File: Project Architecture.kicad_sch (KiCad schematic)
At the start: 32 parts, among them J1 Screw_Terminal_01x04, U1 TMP102xxDRL

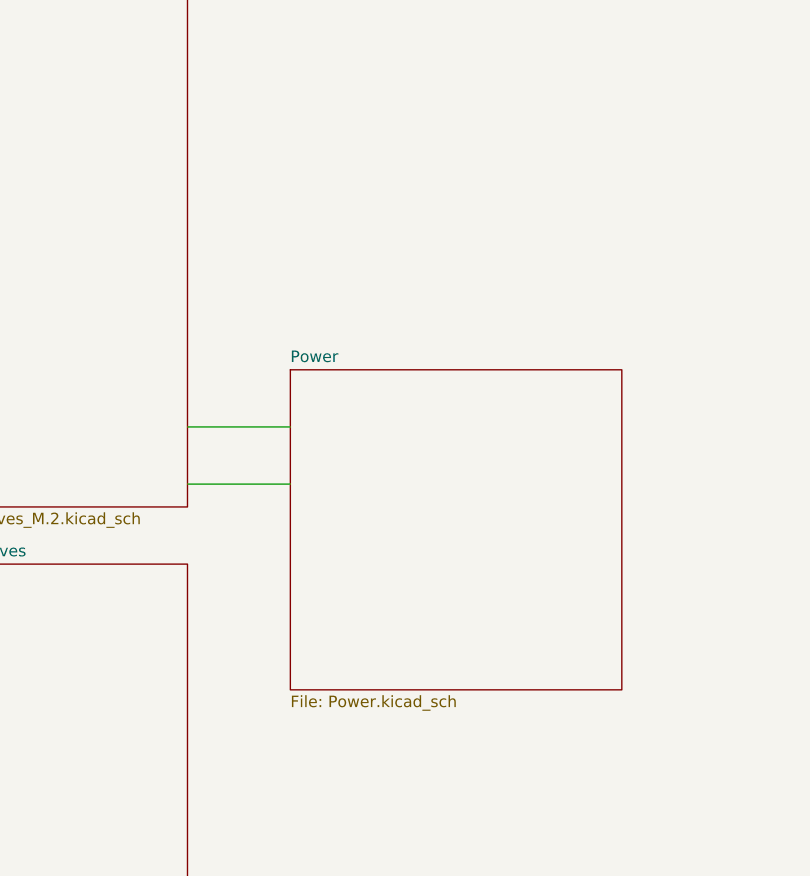
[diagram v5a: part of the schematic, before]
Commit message: Notation changed on M.2 Sheet
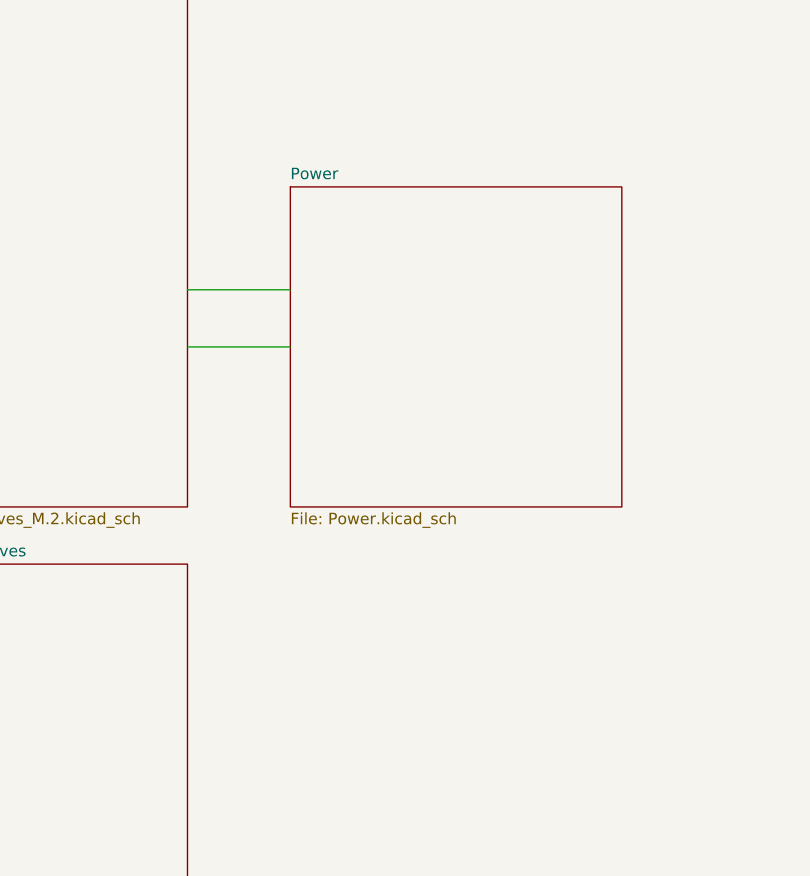
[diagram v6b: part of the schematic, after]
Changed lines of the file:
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@@
 	(wire
 		(pts
-			(xy 287.02 88.9) (xy 298.45 88.9)
+			(xy 287.02 73.66) (xy 298.45 73.66)
 		)
 		(stroke
@@
 	(wire
 		(pts
-			(xy 287.02 82.55) (xy 298.45 82.55)
+			(xy 287.02 67.31) (xy 298.45 67.31)
 		)
 		(stroke
@@
 	)
 	(sheet
-		(at 298.45 76.2)
+		(at 298.45 55.88)
 		(size 36.83 35.56)
 		(exclude_from_sim no)
@@
 		)
 		(property "Sheetname" "Power"
-			(at 298.45 75.4884 0)
+			(at 298.45 55.1684 0)
 			(effects
 				(font
@@
 		)
 		(property "Sheetfile" "Power.kicad_sch"
-			(at 298.45 112.3446 0)
+			(at 298.45 92.0246 0)
 			(effects
 				(font

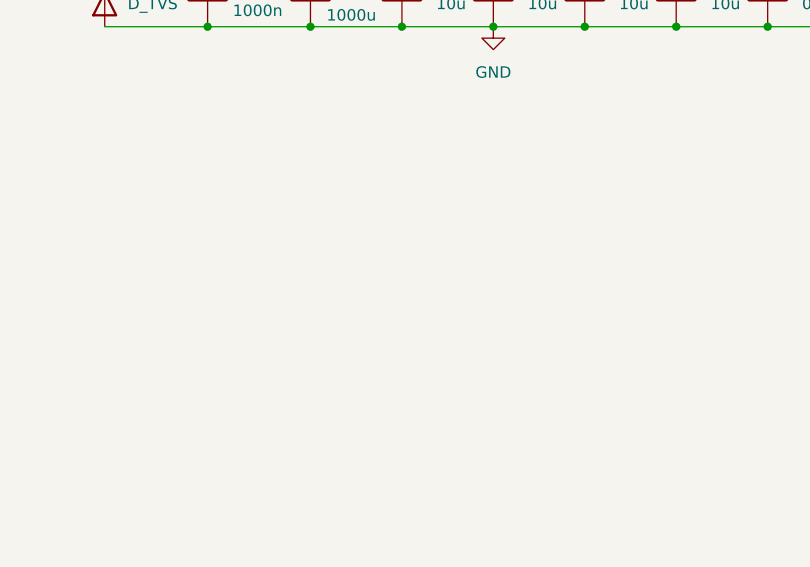
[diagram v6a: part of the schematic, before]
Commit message: Started Ethernet design
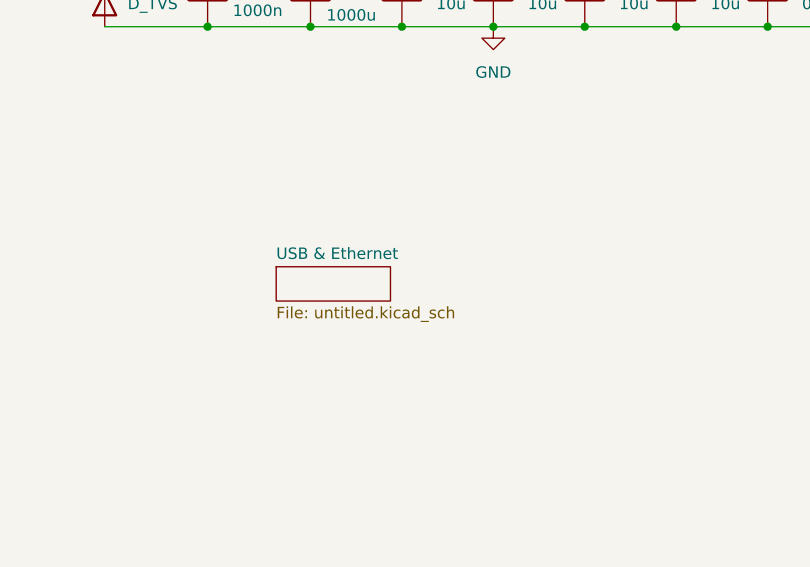
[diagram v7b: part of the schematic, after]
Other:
- added sheet USB & Ethernet (untitled.kicad_sch)
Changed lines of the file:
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@@
+	)
+	(sheet
+		(at 71.12 105.41)
+		(size 12.7 3.81)
+		(exclude_from_sim no)
+		(in_bom yes)
+		(on_board yes)
+		(dnp no)
+		(fields_autoplaced yes)
+		(stroke
+			(width 0.1524)
+			(type solid)
+		)
+		(fill
+			(color 0 0 0 0.0000)
+		)
+		(property "Sheetname" "USB & Ethernet"
+			(at 71.12 104.6984 0)
+			(effects
+				(font
+					(size 1.27 1.27)
+				)
+				(justify left bottom)
+			)
+		)
+		(property "Sheetfile" "untitled.kicad_sch"
+			(at 71.12 109.8046 0)
+			(effects
+				(font
+					(size 1.27 1.27)
+				)
+				(justify left top)
+			)
+		)
+		(instances
+			(project "CM5 Nas"
+				(path "/0650c7a8-acba-429c-9f8e-eec0baf0bc1c/fede4c36-00cc-4d3d-b71c-5243ba232202"
+					(page "10")
+				)
+			)
+		)
 	)
 	(sheet

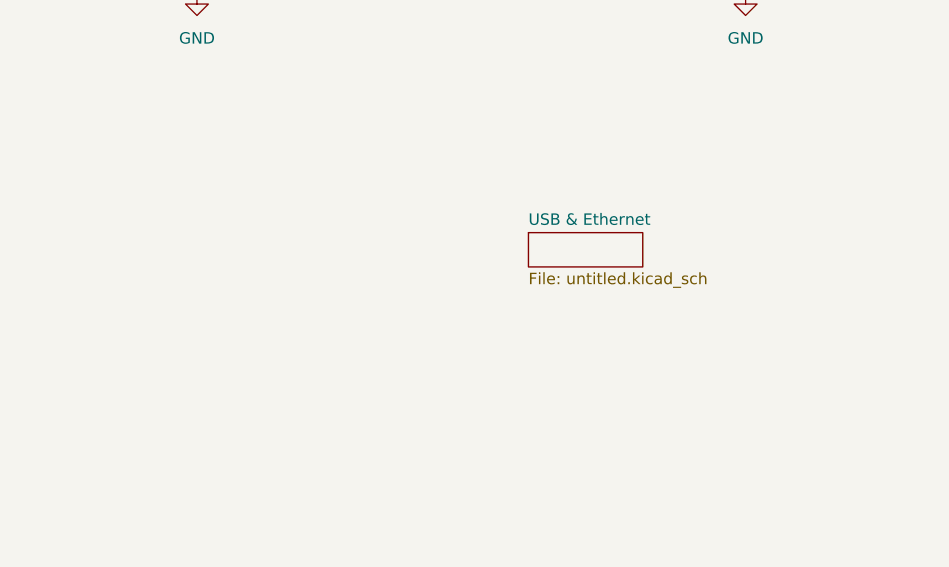
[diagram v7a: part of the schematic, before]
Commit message: Buck converter output voltage changed
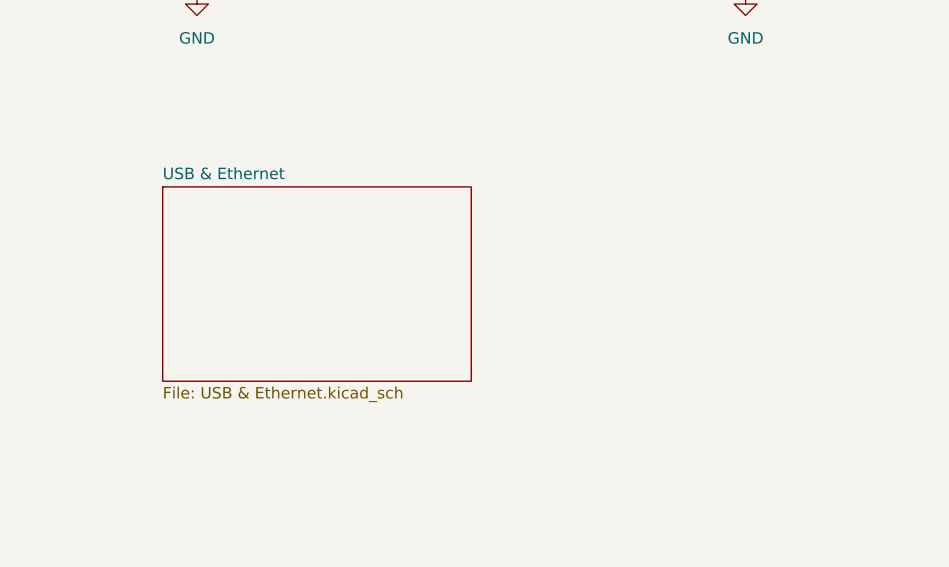
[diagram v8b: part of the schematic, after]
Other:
- sheet USB & Ethernet: file untitled.kicad_sch -> USB & Ethernet.kicad_sch
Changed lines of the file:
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@@
+	)
+	(sheet
+		(at 30.48 100.33)
+		(size 34.29 21.59)
+		(exclude_from_sim no)
+		(in_bom yes)
+		(on_board yes)
+		(dnp no)
+		(fields_autoplaced yes)
+		(stroke
+			(width 0.1524)
+			(type solid)
+		)
+		(fill
+			(color 0 0 0 0.0000)
+		)
+		(property "Sheetname" "USB & Ethernet"
+			(at 30.48 99.6184 0)
+			(effects
+				(font
+					(size 1.27 1.27)
+				)
+				(justify left bottom)
+			)
+		)
+		(property "Sheetfile" "USB & Ethernet.kicad_sch"
+			(at 30.48 122.5046 0)
+			(effects
+				(font
+					(size 1.27 1.27)
+				)
+				(justify left top)
+			)
+		)
+		(instances
+			(project "CM5 Nas"
+				(path "/0650c7a8-acba-429c-9f8e-eec0baf0bc1c/fede4c36-00cc-4d3d-b71c-5243ba232202"
+					(page "10")
+				)
+			)
+		)
 	)
 	(sheet
@@
 				)
 			)
-		)
-	)
-	(sheet
-		(at 71.12 105.41)
-		(size 12.7 3.81)
-		(exclude_from_sim no)
-		(in_bom yes)
-		(on_board yes)
-		(dnp no)
-		(fields_autoplaced yes)
-		(stroke
-			(width 0.1524)
-			(type solid)
-		)
-		(fill
-			(color 0 0 0 0.0000)
-		)
-		(property "Sheetname" "USB & Ethernet"
-			(at 71.12 104.6984 0)
-			(effects
-				(font
-					(size 1.27 1.27)
-				)
-				(justify left bottom)
-			)
-		)
-		(property "Sheetfile" "untitled.kicad_sch"
-			(at 71.12 109.8046 0)
-			(effects
-				(font
-					(size 1.27 1.27)
-				)
-				(justify left top)
-			)
-		)
-		(instances
-			(project "CM5 Nas"
-				(path "/0650c7a8-acba-429c-9f8e-eec0baf0bc1c/fede4c36-00cc-4d3d-b71c-5243ba232202"
-					(page "10")
-				)
-			)
